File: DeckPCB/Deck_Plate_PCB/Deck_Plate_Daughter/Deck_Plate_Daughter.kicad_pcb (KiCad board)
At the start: 2 copper layers, 124.1 x 104 mm, 32 parts, among them J1 SunnyBuddy_Inhibit, J2 JST_Batt_Conn, J3 Motor_Inhibit, J4 BurnWire_Inhibit, J5 Power, J6 Raspberry_Pi_2_3, J7 Board_to_Board, J8 SensorEndPanel, J9 Payload_NextFlex, U2 SunnyBuddy_Breakout, U3 Big_Easy_Driver, U5 Adafruit_INA219_Breakout

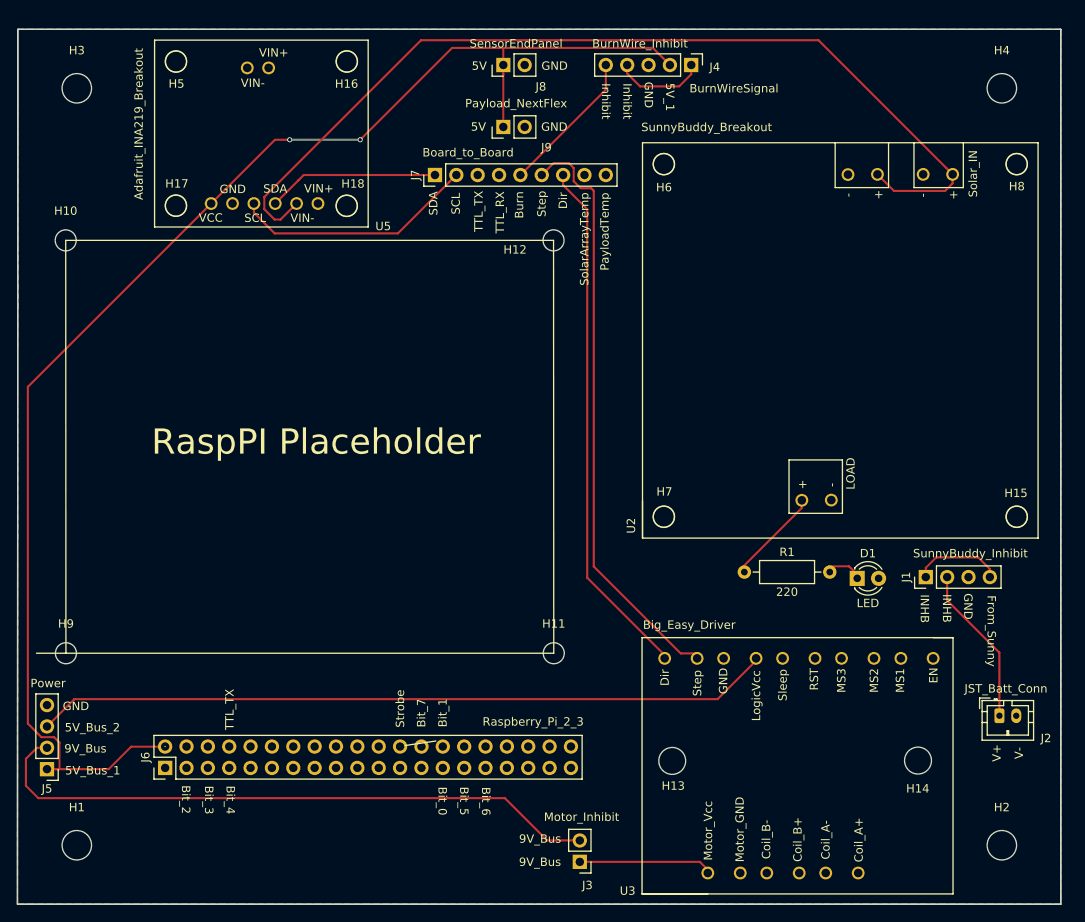
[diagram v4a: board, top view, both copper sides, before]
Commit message: Updated Main_Deck_Plate and Daughter_Board to fit Electronics Enclosure internal dimensions. Created all PCB Gerber files. Created all PCB PNG images. Created all PCB STEP files for mechanical integration. Implemented all design review comments and corrections.
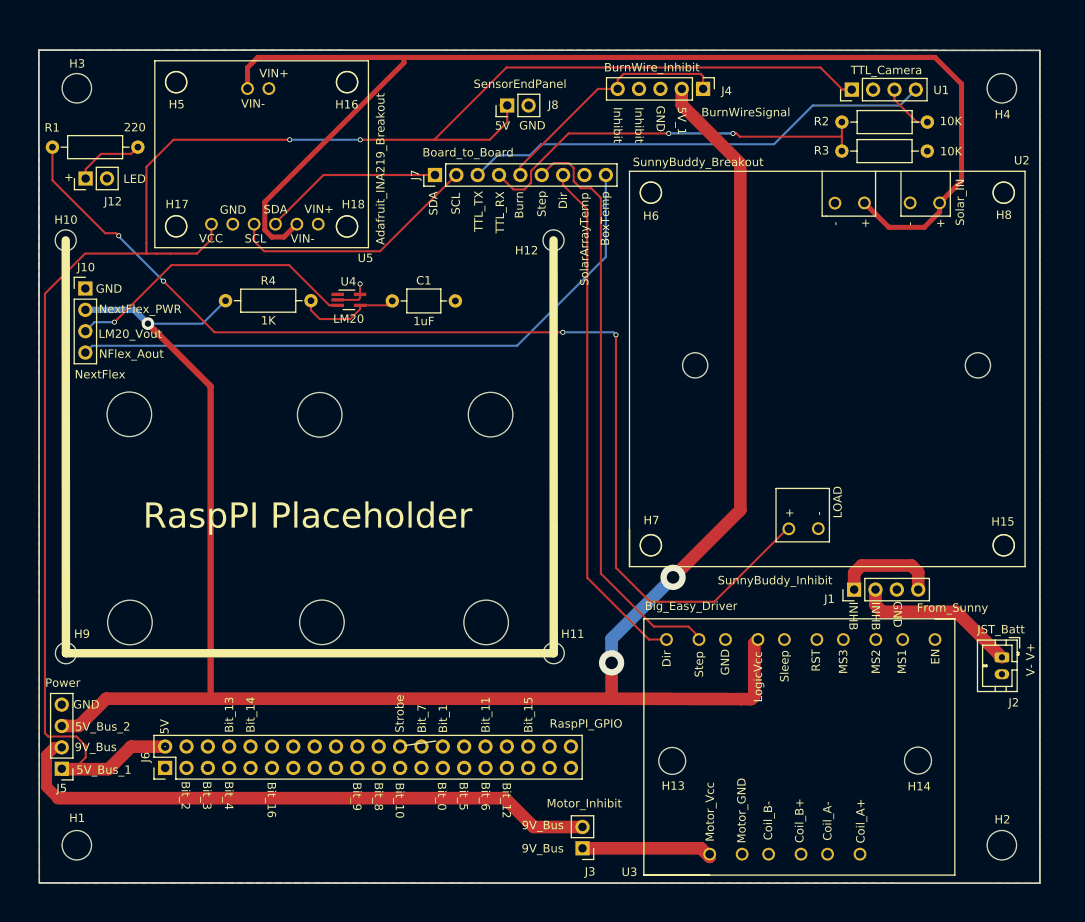
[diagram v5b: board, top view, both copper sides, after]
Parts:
- removed D1: LED, LED_THT:LED_D3.0mm
- removed J9: Payload_NextFlex, Connector_PinHeader_2.54mm:PinHeader_1x02_P2.54mm_Vertical
- added C1: 1uF, Capacitor_THT:C_Axial_L3.8mm_D2.6mm_P7.50mm_Horizontal, F.Cu at (123.5, 75.8)
- added H19: Batt_Holder, MountingHole:MountingHole_5.3mm_M5, F.Cu at (134.6, 114.0)
- added H20: Batt_Holder, MountingHole:MountingHole_5.3mm_M5, F.Cu at (135.1, 89.3)
- added H21: Batt_Holder, MountingHole:MountingHole_5.3mm_M5, F.Cu at (115.1, 114.0)
- added H22: Batt_Holder, MountingHole:MountingHole_5.3mm_M5, F.Cu at (114.8, 89.3)
- added H23: Batt_Holder, MountingHole:MountingHole_5.3mm_M5, F.Cu at (92.2, 89.3)
- added H24: Batt_Holder, MountingHole:MountingHole_5.3mm_M5, F.Cu at (92.2, 114.0)
- added H25: NextFlex_Mount, Deck_Plate_PCB:NextFlex_Mount_3mm, F.Cu at (159.5, 83.5)
- added H26: NextFlex_Mount, Deck_Plate_PCB:NextFlex_Mount_3mm, F.Cu at (193.1, 83.5)
- added J10: NextFlex, Connector_PinHeader_2.54mm:PinHeader_1x04_P2.54mm_Vertical, F.Cu at (87.0, 74.3)
- added J11: NextFlex_BOB, Deck_Plate_PCB:NextFlex, F.Cu at (156.2, 93.0)
- added J12: LED, Connector_PinHeader_2.54mm:PinHeader_1x02_P2.54mm_Vertical, F.Cu at (87.0, 61.2)
- added R2: 10K, Resistor_THT:R_Axial_DIN0207_L6.3mm_D2.5mm_P10.16mm_Horizontal, F.Cu at (176.9, 54.5)
- added R3: 10K, Resistor_THT:R_Axial_DIN0207_L6.3mm_D2.5mm_P10.16mm_Horizontal, F.Cu at (187.1, 58.0)
- added R4: 1K, Resistor_THT:R_Axial_DIN0207_L6.3mm_D2.5mm_P10.16mm_Horizontal, F.Cu at (103.6, 75.8)
- added U1: TTL_Camera, Connector_PinHeader_2.54mm:PinHeader_1x04_P2.54mm_Vertical, F.Cu at (178.1, 50.7)
- added U4: LM20, Package_TO_SOT_SMD:SOT-353_SC-70-5_Handsoldering, F.Cu at (118.3, 75.7)
- J2: value JST_Batt_Conn -> JST_Batt
- J6: value Raspberry_Pi_2_3 -> RaspPI_GPIO
- moved R1 96.6 mm to (83.0, 57.5)
- moved J1 8.65 mm to (178.4, 110.1)
- moved J2 6.95 mm to (195.9, 118.2), turned to 270 degrees
- moved J8 4.83 mm to (137.1, 52.6)
- moved H15 3.74 mm to (196.2, 104.9)
- moved H7 3.73 mm to (154.2, 104.9)
- moved H8 3.73 mm to (196.2, 62.9)
- moved U2 3.73 mm to (198.7, 60.4)
- moved H6 3.72 mm to (154.2, 62.9)
- moved J4 3.17 mm to (160.4, 50.6)
- moved H16 2.46 mm to (118.1, 49.8)
- moved U5 2.46 mm to (95.2, 47.2)
- moved H5 2.45 mm to (97.8, 49.8)
- moved H18 2.45 mm to (118.1, 67.0)
- moved H17 2.45 mm to (97.8, 66.9)
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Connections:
- J4 pad 2: /5V_Bus_1 -> /5V_Bus_2
- J7 pad 9: /PayloadTemp -> /Box_Temp
- R1 pad 2: Net-(D1-Pad1) -> /LED+
- U5 pad 7: (no net) -> /Solar_IN+
- U5 pad 8: (no net) -> /SolarCell+
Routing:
- net /5V_Bus_2: track 88.3 -> 239.3 mm, vias 0 -> 3
- net Net-(R1-Pad1): track 10.7 -> 132.1 mm, vias 0 -> 4
- net /Box_Temp: track 0.00 -> 76.4 mm
- net /TTL_TX: track 0.00 -> 56.3 mm
- net /TTL_RX: track 0.00 -> 48.7 mm, vias 0 -> 2
- net /5V_Bus_1: track 167.8 -> 211.3 mm
- net /LM20_Vout: track 0.00 -> 35.2 mm, vias 0 -> 1
- net /Solar_IN+: track 114.0 -> 148.6 mm
- net Net-(C1-Pad1): track 0.00 -> 12.4 mm
- net /LED+: track 0.00 -> 8.40 mm
- net Net-(R2-Pad2): track 0.00 -> 6.21 mm
- net GND: track 0.00 -> 4.44 mm, vias 0 -> 1
- net Net-(D1-Pad1): track 3.45 -> 0.00 mm
- net /9V_Bus: track 90.1 -> 87.5 mm
- net /Sunny_Batt_Out: track 10.8 -> 12.4 mm
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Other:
- board size 124.1 x 104 mm -> 119 x 99.1 mm
- board text added: "+"
- board text added: "Battery Placement"
- board text added: "Bit_10"
- board text added: "Bit_11"
- board text added: "Bit_12"
- board text added: "Bit_13"
- board text added: "Bit_14"
- board text added: "Bit_15"
- board text added: "Bit_16"
- board text added: "Bit_8"
- board text added: "Bit_9"
- board text added: "BoxTemp"
- board text added: "LM20_Vout"
- board text added: "NFlex_Aout"
- board text added: "NextFlex_PWR"
- board text removed: "PayloadTemp"

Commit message: Updated Main_Board and Daughter_Board to have rounded off corners to fit inside of the Electronics Enclosure. Verified with CAD model of electronics enclosure.
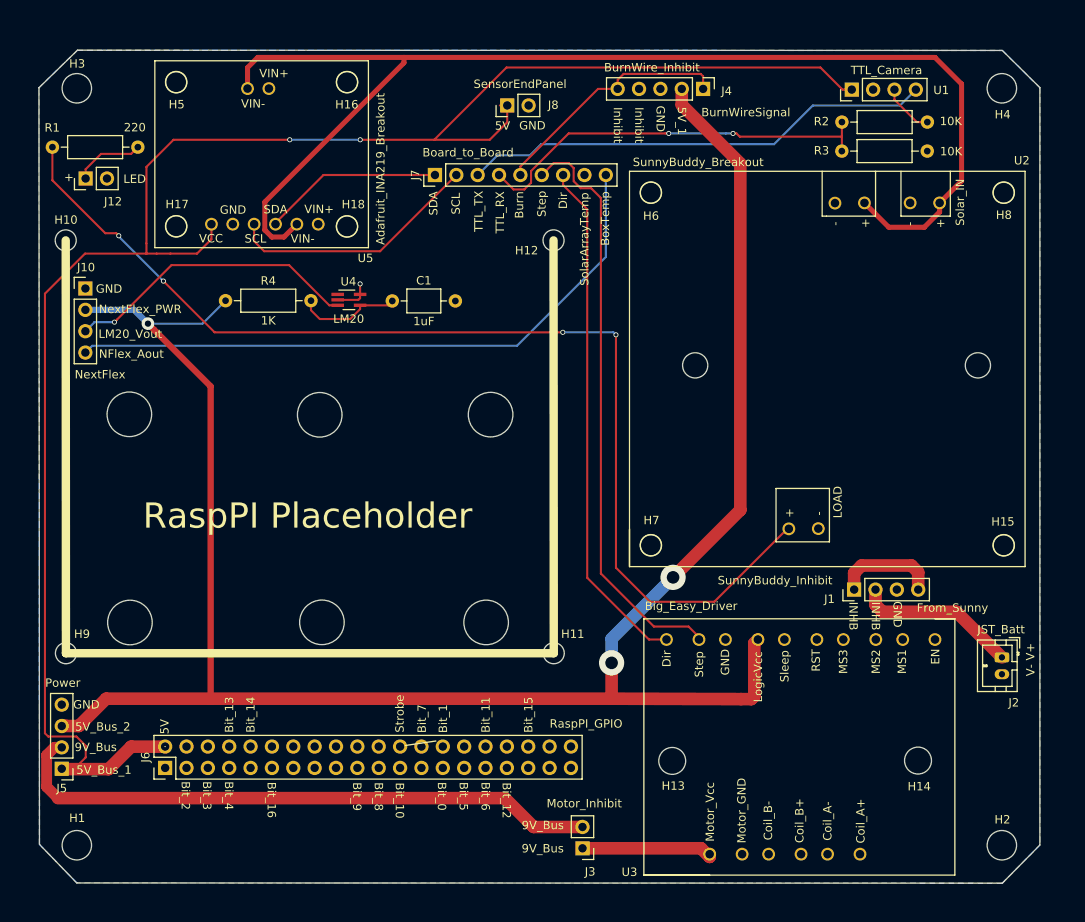
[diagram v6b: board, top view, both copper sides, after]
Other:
- outline, holes or cut-outs redrawn
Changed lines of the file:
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@@
       (psa4output false)
       (plotreference true)
-      (plotvalue false)
+      (plotvalue true)
       (plotinvisibletext false)
       (padsonsilk false)
@@
     (pad 1 np_thru_hole circle (at 0 0) (size 3.5 3.5) (drill 3.5) (layers *.Cu *.Mask))
   )
-  (gr_line (start 81.48 145.02) (end 200.46 145.06) (layer Edge.Cuts) (width 0.15))
-  (gr_line (start 81.42 45.98) (end 81.48 145.02) (layer Edge.Cuts) (width 0.15))
-  (gr_line (start 200.46 46.02) (end 81.42 45.98) (layer Edge.Cuts) (width 0.15))
-  (gr_line (start 200.46 145.06) (end 200.46 46.02) (layer Edge.Cuts) (width 0.15))
+  (gr_line (start 195.99 145.05) (end 200.46 140.52) (layer Edge.Cuts) (width 0.15))
+  (gr_line (start 85.93 145.02) (end 195.99 145.05) (layer Edge.Cuts) (width 0.15))
+  (gr_line (start 81.49 140.44) (end 85.93 145.02) (layer Edge.Cuts) (width 0.15))
+  (gr_line (start 81.43 50.46) (end 81.49 140.44) (layer Edge.Cuts) (width 0.15))
+  (gr_line (start 86.01 45.99) (end 81.43 50.46) (layer Edge.Cuts) (width 0.15))
+  (gr_line (start 195.99 46.02) (end 86.01 45.99) (layer Edge.Cuts) (width 0.15))
+  (gr_line (start 200.46 50.44) (end 195.99 46.02) (layer Edge.Cuts) (width 0.15))
+  (gr_line (start 200.46 140.52) (end 200.46 50.44) (layer Edge.Cuts) (width 0.15))
   (gr_text Bit_15 (at 139.65 125.03 90) (layer F.SilkS)
     (effects (font (size 1 1) (thickness 0.15)))
@@
     (effects (font (size 1 1) (thickness 0.15)))
   )
-  (gr_line (start 81.48 145.02) (end 200.46 145.06) (layer F.SilkS) (width 0.15))
-  (gr_line (start 81.42 45.98) (end 81.48 145.02) (layer F.SilkS) (width 0.15))
-  (gr_line (start 200.46 46.02) (end 81.42 45.98) (layer F.SilkS) (width 0.15))
-  (gr_line (start 200.46 145.06) (end 200.46 46.02) (layer F.SilkS) (width 0.15))
   (gr_text Dir (at 143.764 63.881 90) (layer F.SilkS)
     (effects (font (size 1 1) (thickness 0.15)))
@@
     (polygon
       (pts
-        (xy 200.46 46.02) (xy 200.46 145.06) (xy 81.48 145.02) (xy 81.42 45.98)
+        (xy 195.99 46.02) (xy 200.46 50.44) (xy 200.46 140.52) (xy 196 145.05) (xy 85.93 145.02)
+        (xy 81.49 140.44) (xy 81.43 50.45) (xy 86.01 45.99)
       )
     )
